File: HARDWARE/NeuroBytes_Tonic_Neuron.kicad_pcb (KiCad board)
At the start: 2 copper layers, 51.9 x 18 mm, 28 parts, among them P1 CONN_01X04, P2 CONN_01X04, P3 CONN_01X04, P4 JST_GH_5-pos, Q1 Q_NPN_BEC, Q2 Q_NPN_BEC, Q3 Q_NPN_BEC, SW1 SW_PUSH, U1 STM32L011Gx, U2 LD3985G33R

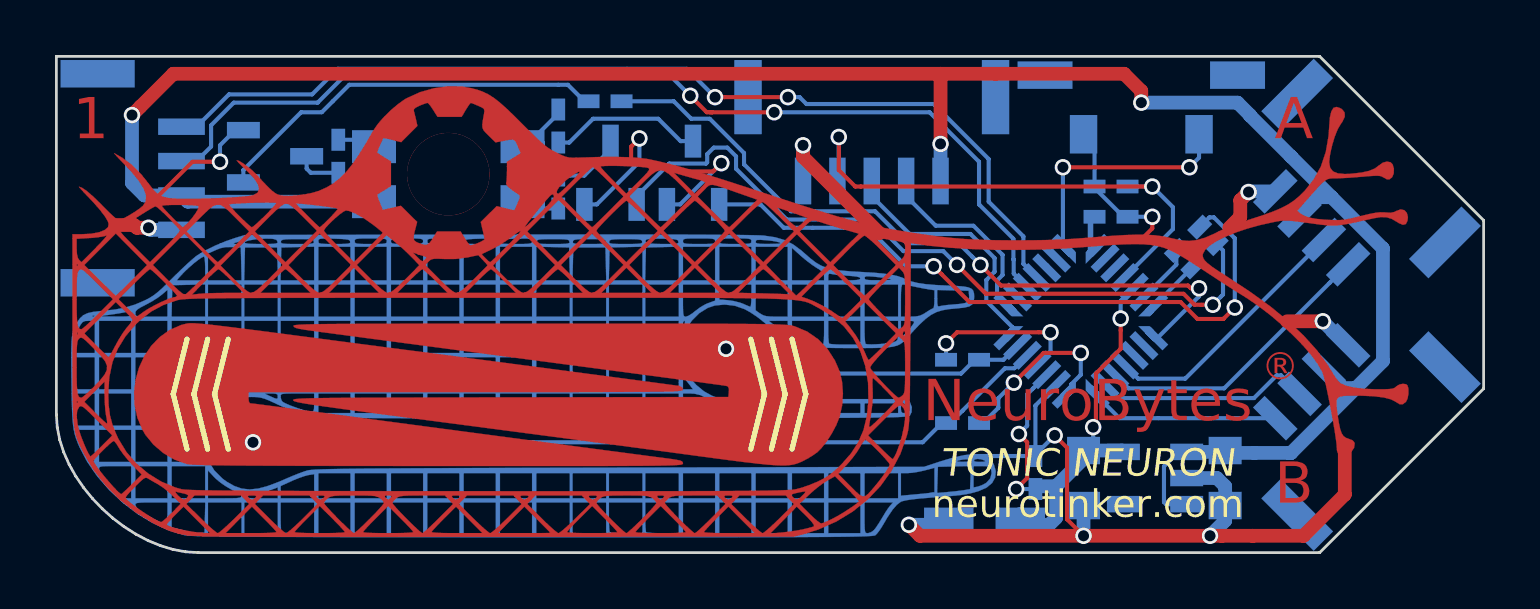
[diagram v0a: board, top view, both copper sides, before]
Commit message: changed to RClamp0503F for ESD protection (touch slider, switch, 3v3). ordered 30 PCBs.
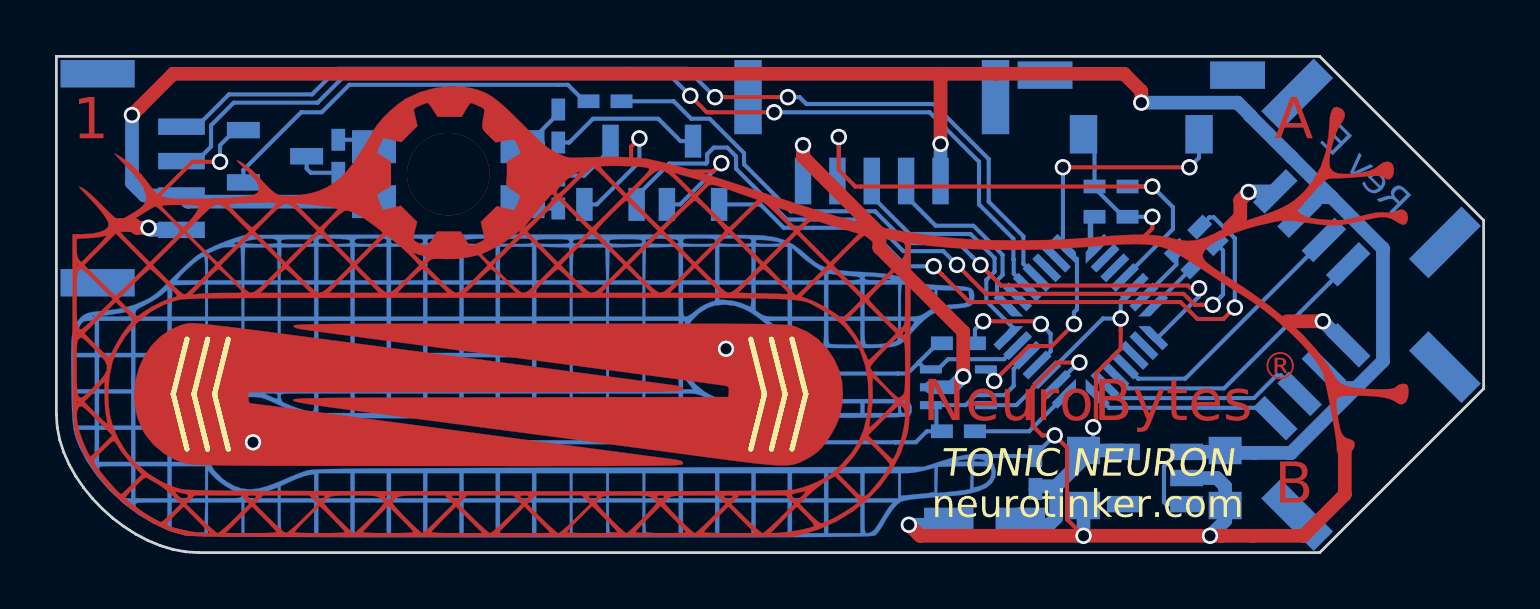
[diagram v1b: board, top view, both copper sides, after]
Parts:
- added U3: RClamp0503F, KiCad_Footprints:ZF_SMD_SOT-353, B.Cu at (186.1, 73.0)
- U2: value LD3985G33R -> TLV70033_SOT23-5
- moved R3 0.62 mm to (186.1, 71.4), turned to 0 degrees
- moved R2 0.34 mm to (186.1, 74.6)
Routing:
- net GND: track 67.3 -> 78.0 mm, vias 12 -> 14
- net Net-(SW1-Pad2): track 9.36 -> 16.5 mm, vias 2 -> 4
- net Net-(R2-Pad2): track 6.43 -> 3.73 mm, vias 2 -> 0
- net Net-(R3-Pad1): track 11.4 -> 13.0 mm
- net Net-(R2-Pad1): track 29.5 -> 30.9 mm
- net Net-(R3-Pad2): track 5.96 -> 4.91 mm
- net +3V3: track 19.3 -> 19.8 mm, vias 4 -> 2
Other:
- board text added: "Rev E"
